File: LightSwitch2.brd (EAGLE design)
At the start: 22 x 44 mm, 3 parts, among them SW1 SWITCH-SPDT-ILLUMINATED, SW2 SWITCH-SPDT-ILLUMINATED

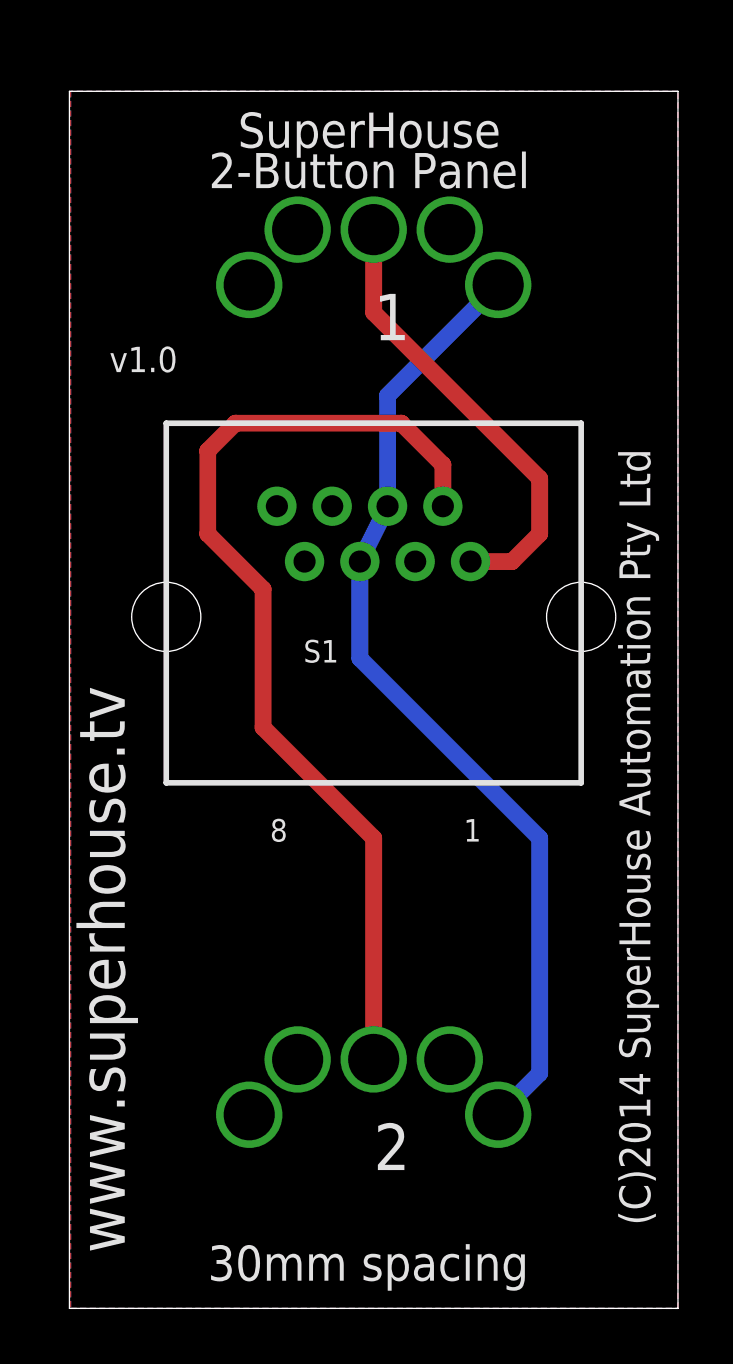
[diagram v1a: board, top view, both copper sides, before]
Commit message: Replaced buttons with more common SPST type
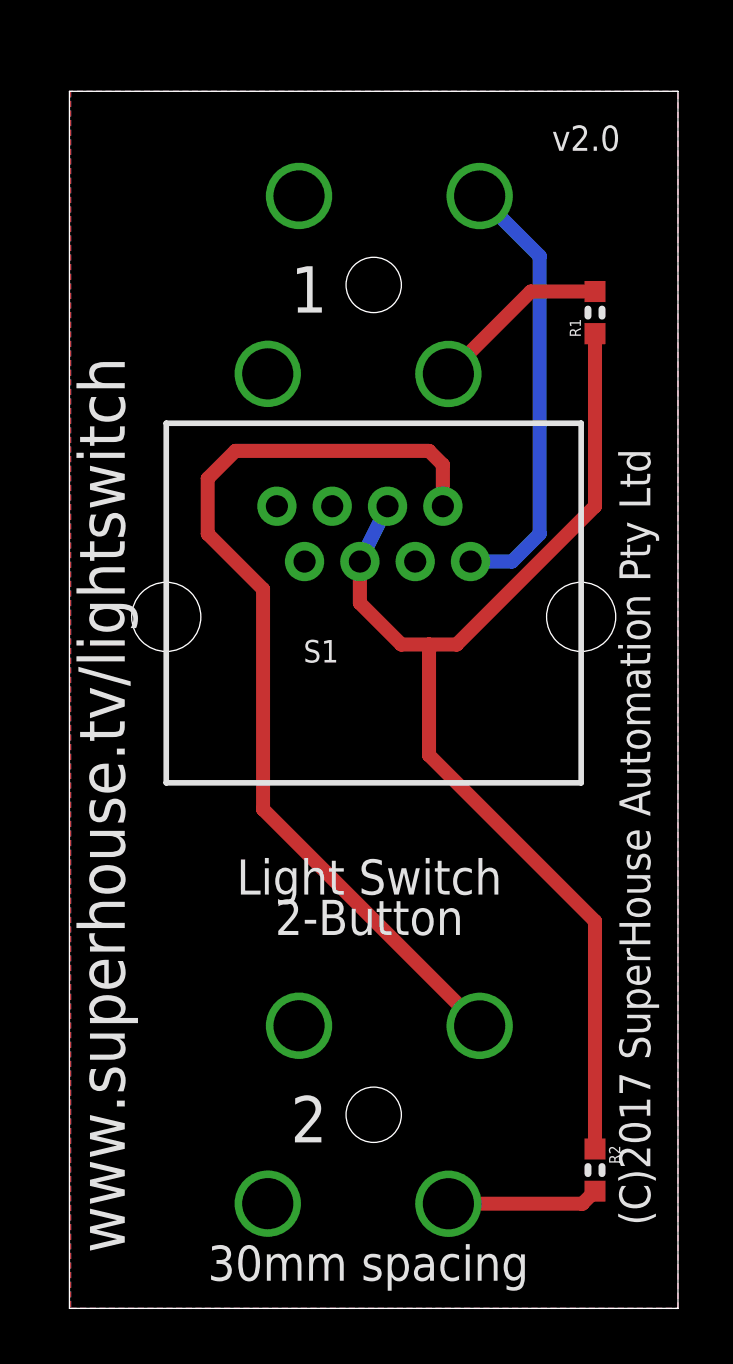
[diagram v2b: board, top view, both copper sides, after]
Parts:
- added R1, R2: 3K3, freetronics-jon:0603
- SW1, SW2: value SWITCH-SPDT-ILLUMINATED -> SWITCH-SPST-ILLUMINATED; device freetronics-jon:SWITCH-SPDT-ILLUMINATED -> freetronics-jon:SWITCH-SPST-ILLUMINATED
- turned SW1 to 50 degrees
- turned SW2 to 50 degrees
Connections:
- new net N$1: R1.2, SW1.2
- new net N$2: R2.2, SW2.2
- net +12V: now also R1.1, R2.1; no longer SW1.1, SW2.1
- net GND: now also SW1.1, SW1.4, SW2.1, SW2.4; no longer SW1.2, SW1.5, SW2.2, SW2.5
- net N$4: now also SW1.3; no longer SW1.4
- net N$5: now also SW2.3; no longer SW2.4
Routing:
- net +12V: track 35.2 -> 41.9 mm
- net N$1: track 0.00 -> 6.53 mm
- net N$2: track 0.00 -> 5.49 mm
- net N$5: track 35.5 -> 34.5 mm
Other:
- board text added: "(C)2017 SuperHouse Automation Pty Ltd"
- board text added: "Light Switch 2-Button"
- board text added: "v2.0"
- board text added: "www.superhouse.tv/lightswitch"
- board text removed: "(C)2014 SuperHouse Automation Pty Ltd"
- board text removed: "8"
- board text removed: "SuperHouse 2-Button Panel"
- board text removed: "v1.0"
- board text removed: "www.superhouse.tv"
